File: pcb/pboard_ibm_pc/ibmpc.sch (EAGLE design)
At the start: 49 parts, among them IC1 STM32F072C8T6, SW1 324_SW, SW4 324_SW, U1 MAX3232

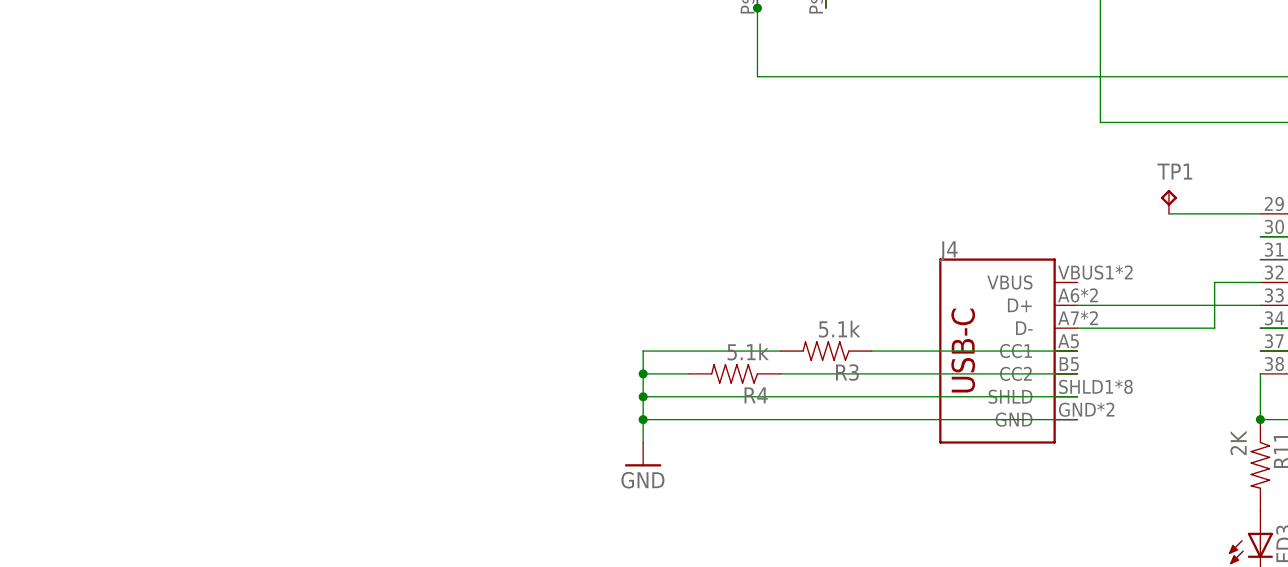
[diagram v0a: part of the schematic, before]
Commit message: finished ADB protocol board
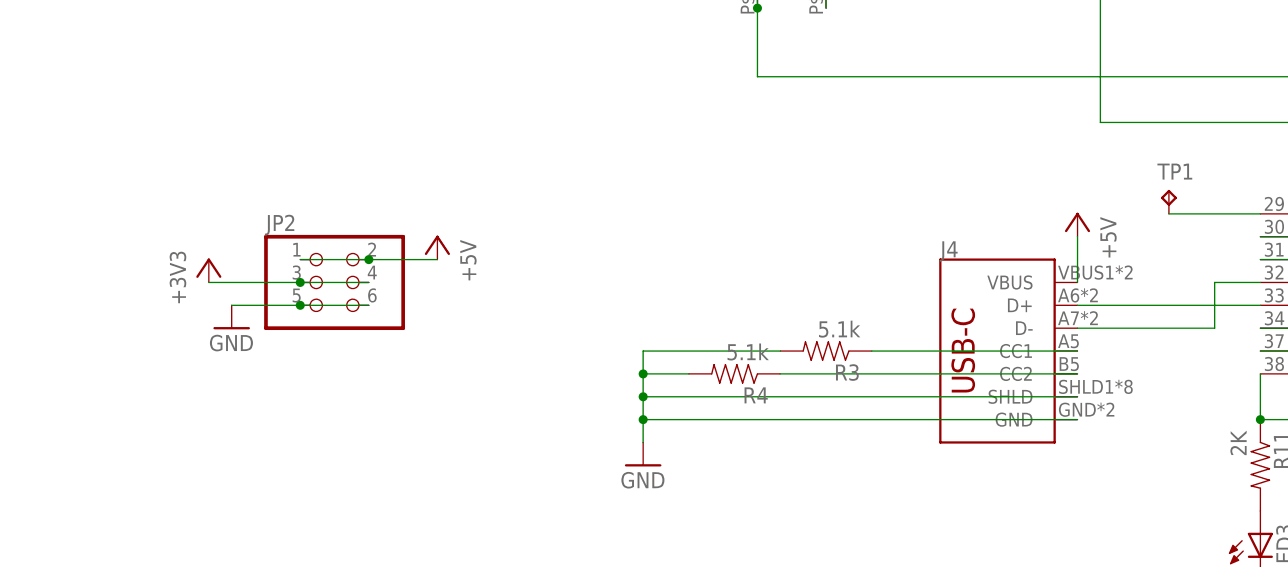
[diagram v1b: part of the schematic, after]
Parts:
- added JP2: (no value), pinhead:PINHD-2X3
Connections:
- net +3V3: now also JP2.3, JP2.4
- net +5V: now also J4.VBUS, JP2.1, JP2.2
- net GND: now also JP2.5, JP2.6
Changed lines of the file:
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@@
 <part name="+3V9" library="backplane" deviceset="+3V3" device=""/>
 <part name="+3V12" library="backplane" deviceset="+3V3" device=""/>
+<part name="P+2" library="supply1" library_urn="urn:adsk.eagle:library:371" deviceset="+5V" device=""/>
+<part name="JP2" library="pinhead" library_urn="urn:adsk.eagle:library:325" deviceset="PINHD-2X3" device="" package3d_urn="urn:adsk.eagle:package:22462/2"/>
+<part name="P+3" library="supply1" library_urn="urn:adsk.eagle:library:371" deviceset="+5V" device=""/>
+<part name="GND17" library="supply1" library_urn="urn:adsk.eagle:library:371" deviceset="GND" device=""/>
+<part name="+3V13" library="supply1" library_urn="urn:adsk.eagle:library:371" deviceset="+3V3" device=""/>
 </parts>
 <sheets>
@@
 <attribute name="VALUE" x="139.7" y="172.72" size="1.778" layer="96"/>
 </instance>
+<instance part="P+2" gate="1" x="20.32" y="-38.1" smashed="yes" rot="MR0">
+<attribute name="VALUE" x="22.86" y="-43.18" size="1.778" layer="96" rot="MR90"/>
+</instance>
+<instance part="JP2" gate="A" x="-63.5" y="-45.72" smashed="yes">
+<attribute name="NAME" x="-69.85" y="-40.005" size="1.778" layer="95"/>
+<attribute name="VALUE" x="-69.85" y="-53.34" size="1.778" layer="96"/>
+</instance>
+<instance part="P+3" gate="1" x="-50.8" y="-40.64" smashed="yes" rot="MR0">
+<attribute name="VALUE" x="-48.26" y="-45.72" size="1.778" layer="96" rot="MR90"/>
+</instance>
+<instance part="GND17" gate="1" x="-73.66" y="-50.8" smashed="yes">
+<attribute name="VALUE" x="-76.2" y="-53.34" size="1.778" layer="96"/>
+</instance>
+<instance part="+3V13" gate="G$1" x="-76.2" y="-43.18" smashed="yes">
+<attribute name="VALUE" x="-78.74" y="-48.26" size="1.778" layer="96" rot="R90"/>
+</instance>
 </instances>
 <busses>
@@
 <pinref part="+3V9" gate="G$1" pin="+3V3"/>
 <wire x1="106.68" y1="167.64" x2="111.76" y2="167.64" width="0.1524" layer="91"/>
+</segment>
+<segment>
+<pinref part="JP2" gate="A" pin="3"/>
+<pinref part="+3V13" gate="G$1" pin="+3V3"/>
+<wire x1="-66.04" y1="-45.72" x2="-76.2" y2="-45.72" width="0.1524" layer="91"/>
+<pinref part="JP2" gate="A" pin="4"/>
+<wire x1="-66.04" y1="-45.72" x2="-58.42" y2="-45.72" width="0.1524" layer="91"/>
+<junction x="-66.04" y="-45.72"/>
 </segment>
 </net>
@@
 <wire x1="20.32" y1="93.98" x2="20.32" y2="81.28" width="0.1524" layer="91"/>
 </segment>
+<segment>
+<pinref part="GND17" gate="1" pin="GND"/>
+<pinref part="JP2" gate="A" pin="5"/>
+<wire x1="-73.66" y1="-48.26" x2="-66.04" y2="-48.26" width="0.1524" layer="91"/>
+<pinref part="JP2" gate="A" pin="6"/>
+<wire x1="-66.04" y1="-48.26" x2="-58.42" y2="-48.26" width="0.1524" layer="91"/>
+<junction x="-66.04" y="-48.26"/>
+</segment>
 </net>
 <net name="N$29" class="0">
@@
 <junction x="114.3" y="43.18"/>
 </segment>
-</net>
+<segment>
+<pinref part="P+2" gate="1" pin="+5V"/>
+<pinref part="J4" gate="J1" pin="VBUS"/>
+<wire x1="20.32" y1="-40.64" x2="20.32" y2="-45.72" width="0.1524" layer="91"/>
+</segment>
+<segment>
+<pinref part="P+3" gate="1" pin="+5V"/>
+<pinref part="JP2" gate="A" pin="2"/>
+<wire x1="-50.8" y1="-43.18" x2="-58.42" y2="-43.18" width="0.1524" layer="91"/>
+<pinref part="JP2" gate="A" pin="1"/>
+<wire x1="-58.42" y1="-43.18" x2="-66.04" y2="-43.18" width="0.1524" layer="91"/>
+<junction x="-58.42" y="-43.18"/>
+</segment>
+</net>

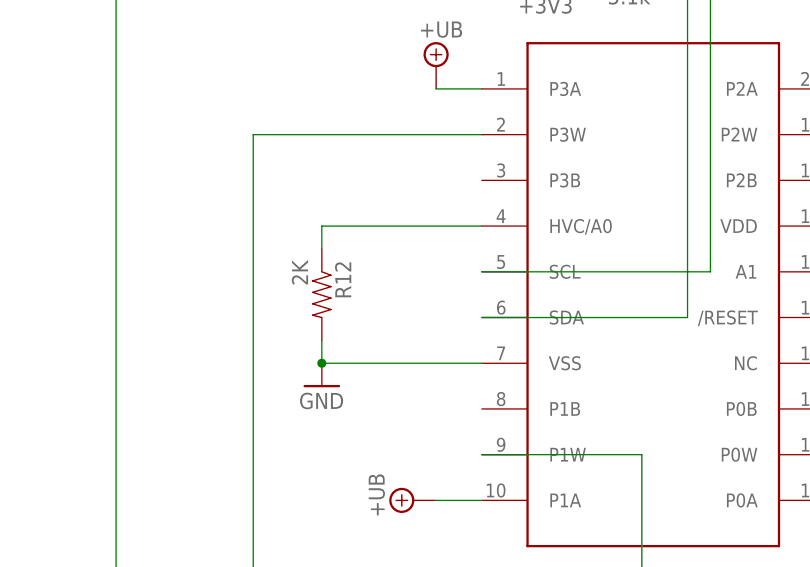
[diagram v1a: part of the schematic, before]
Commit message: added dsub stacker board
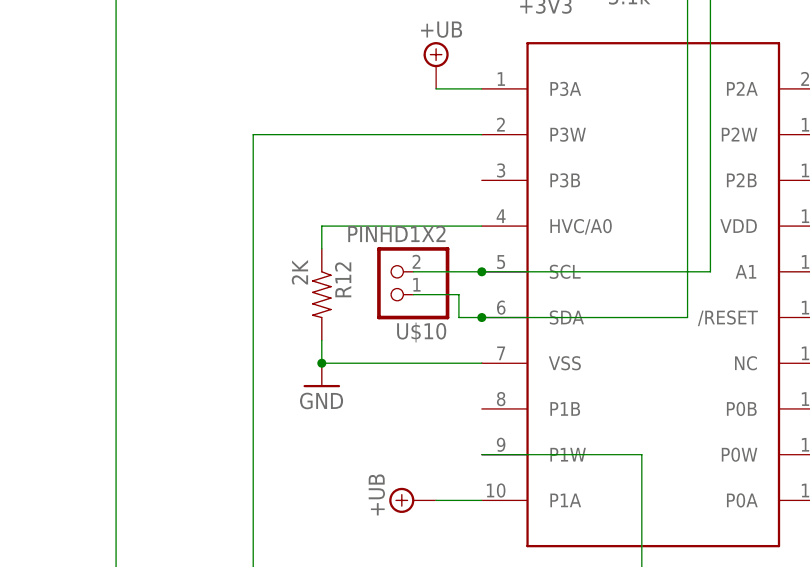
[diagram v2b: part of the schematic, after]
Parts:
- added U$10: PINHD1X2, adafruit_changed:PINHD1X2
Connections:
- removed net N$30: IC1PORTB_H.PB14, R14.2, U$6.SDA
- removed net N$31: IC1PORTB_H.PB13, R13.2, U$6.SCL
- new net POT_SCL: IC1PORTB_H.PB13, R13.2, U$10.2, U$6.SCL
- new net PST_SDA: IC1PORTB_H.PB14, R14.2, U$10.1, U$6.SDA
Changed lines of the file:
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@@
 <part name="GND17" library="supply1" library_urn="urn:adsk.eagle:library:371" deviceset="GND" device=""/>
 <part name="+3V13" library="supply1" library_urn="urn:adsk.eagle:library:371" deviceset="+3V3" device=""/>
+<part name="U$10" library="adafruit_changed" deviceset="PINHD1X2" device=""/>
 </parts>
 <sheets>
@@
 <attribute name="VALUE" x="-78.74" y="-48.26" size="1.778" layer="96" rot="R90"/>
 </instance>
+<instance part="U$10" gate="1" x="88.9" y="134.62" smashed="yes" rot="R180">
+<attribute name="NAME" x="95.25" y="128.905" size="1.778" layer="95" rot="R180"/>
+<attribute name="VALUE" x="95.25" y="139.7" size="1.778" layer="96" rot="R180"/>
+</instance>
 </instances>
 <busses>
@@
 </segment>
 </net>
-<net name="N$30" class="0">
+<net name="PST_SDA" class="0">
 <segment>
 <pinref part="IC1" gate="PORTB_H" pin="PB14"/>
@@
 <pinref part="R14" gate="G$1" pin="2"/>
 <junction x="121.92" y="167.64"/>
-</segment>
-</net>
-<net name="N$31" class="0">
+<wire x1="99.06" y1="129.54" x2="96.52" y2="129.54" width="0.1524" layer="91"/>
+<wire x1="96.52" y1="129.54" x2="96.52" y2="132.08" width="0.1524" layer="91"/>
+<junction x="99.06" y="129.54"/>
+<pinref part="U$10" gate="1" pin="1"/>
+<wire x1="96.52" y1="132.08" x2="91.44" y2="132.08" width="0.1524" layer="91"/>
+</segment>
+</net>
+<net name="POT_SCL" class="0">
 <segment>
 <pinref part="IC1" gate="PORTB_H" pin="PB13"/>
@@
 <pinref part="R13" gate="G$1" pin="2"/>
 <junction x="124.46" y="170.18"/>
-</segment>
-</net>
+<pinref part="U$10" gate="1" pin="2"/>
+<wire x1="99.06" y1="134.62" x2="91.44" y2="134.62" width="0.1524" layer="91"/>
+<junction x="99.06" y="134.62"/>
+</segment>
+</net>

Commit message: finishing touches for new boards
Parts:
- removed SW4: 324_SW, 3pos_slide_switch_centered:324_SW
- removed TP4: TPTP12R, testpad:TPTP12R
- added R15: 2K, SparkFun-Passives:RESISTOR0805-RES
- added SW2: 324_SW, 3pos_slide_switch_centered:324_SW
- C3: value 1uF -> 100nF
- C9: value 100nF -> 1uF
- J2: device SparkFun-Connectors:DIN7 -> SparkFun-Connectors:DB9MALE
- J3: device SparkFun-Connectors:DB9MALE -> SparkFun-Connectors:DIN7
- R1: value 12K -> 5.1k
- R11, R9: value 2K -> 12K
- R2: value 2K -> 5.1k
- R3, R4: value 5.1k -> 2K
- R5: value 12K -> 2K
- U$1: value GAMEPORT_15P -> PINHD1X4; device ibmpc:GAMEPORT_15P -> adafruit_changed:PINHD1X4
- U$10: value PINHD1X2 -> PINHD1X4; device adafruit_changed:PINHD1X2 -> adafruit_changed:PINHD1X4
- U$4: value M2.5HOLE -> PINHD1X2; device f1c100s:M2.5HOLE -> adafruit_changed:PINHD1X2
- U$5: value M2.5HOLE -> MCP4451; device f1c100s:M2.5HOLE -> ps2:MCP4451
- U$6: value MCP4451 -> M2.5HOLE; device ps2:MCP4451 -> f1c100s:M2.5HOLE
- U$7: value PINHD1X4 -> M2.5HOLE; device adafruit_changed:PINHD1X4 -> f1c100s:M2.5HOLE
- U$9: value PINHD1X4 -> GAMEPORT_15P; device adafruit_changed:PINHD1X4 -> ibmpc:GAMEPORT_15P
- renumbered JP4 to JP3
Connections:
- removed net N$35: U$1.Y1, U$6.P2W
- removed net N$36: U$1.Y2, U$6.P3W
- new net N$30: U$5.P1W, U$9.Y2
- new net N$31: IC1PORTF/OSC.PF1/OSC=>, R5.1, U$9.B1
- net +3V3: now also C1.1, C6.2, C7.2, C9.2, LED1.A, R1.1, R2.1, R3.1, R9.2, SW2.2, SW2.3, U$5.VDD; no longer C1.2, C2.2, C3.2, C7.1, LED2.A, R1.2, R13.1, R14.1, SW1.2, SW1.3, U$6.VDD
- net +UB: now also R5.2, R6.2, U$5.P0A, U$5.P1A, U$5.P2A, U$5.P3A, U$9.5V_1, U$9.5V_2, U$9.5V_3; no longer R7.2, R9.2, U$1.5V_1, U$1.5V_2, U$1.5V_3, U$6.P0A, U$6.P1A, U$6.P2A, U$6.P3A
- net C1+: now also C3.1; no longer C9.1
- net C1-: now also C3.2; no longer C9.2
- net C2+: now also C5.1; no longer C4.1
- net C2-: now also C5.2; no longer C4.2
- net GND: now also C1.2, C2.2, C4.2, C6.1, C7.1, C9.1, J2.5, J3.3_GND, LED2.C, R11.1, R13.2, R14.2, R7.1, SW1.1, SW1.4, U$1.4, U$5.A1, U$5.VSS, U$9.GND_B1, U$9.GND_B2; no longer C1.1, C2.1, C3.1, C5.2, C6.2, C7.2, J2.3_GND, J3.5, LED1.C, R12.2, R3.2, R5.1, R6.1, SW4.1, SW4.4, U$1.GND_B1, U$1.GND_B2, U$6.A1, U$6.VSS, U$7.4
- net N$1: now also R13.1; no longer R3.1
- net N$10: now also J1.1_DATA, U$1.2; no longer J2.1_DATA, U$8.2
- net N$11: now also J1.5_CLK, U$1.3; no longer J2.5_CLK, U$8.3
- net N$13: now also R9.1, SW1.2, SW1.3; no longer R1.1, SW4.2, SW4.3
- net N$17: now also U$5.P0W, U$9.Y1; no longer IC1PORTC.PC14, R7.1, U$1.B1
- net N$18: now also R11.2, SW2.1, SW2.4; no longer R5.2, SW1.1, SW1.4
- net N$19: now also IC1PORTC.PC15, R6.1, U$9.B2; no longer IC1PORTF/OSC.PF0/OSC<=, R8.1, U$1.B2
- net N$2: now also LED2.A, R12.2; no longer LED1.A, R2.2
- net N$20: now also IC1PORTF/OSC.PF0/OSC<=, R8.1, U$9.B3; no longer IC1PORTC.PC15, R9.1, U$1.B3
- net N$21: now also IC1PORTC.PC14, U$9.B4; no longer IC1PORTF/OSC.PF1/OSC=>, U$1.B4
- net N$25: now also J2.8; no longer J3.8
- net N$26: now also J3.1_DATA, U$8.2; no longer J1.1_DATA, U$7.2
- net N$27: now also R15.1; no longer R11.1
- net N$28: now also R15.2; no longer R11.2
- net N$29: now also LED1.C, R7.2; no longer LED2.C, R6.2
- net N$3: now also J3.4_5V, U$8.1; no longer J1.4_5V, U$7.1
- net N$32: now also R4.1, U$5.HVC/A0; no longer R12.1, U$6.HVC/A0
- net N$33: now also U$5.P2W, U$9.X2; no longer U$1.X1, U$6.P0W
- net N$34: now also U$5.P3W, U$9.X1; no longer U$1.X2, U$6.P1W
- net N$38: now also U$10.1; no longer U$9.1
- net N$39: now also U$10.2; no longer U$9.2
- net N$4: now also J1.4_5V, U$1.1; no longer J2.4_5V, U$8.1
- net N$40: now also U$10.3; no longer U$9.3
- net N$41: now also U$10.4; no longer U$9.4
- net N$44: now also R3.2, U$5./RESET; no longer TP4.TP
- net N$5: now also J3.5_CLK, U$8.3; no longer J1.5_CLK, U$7.3
- net N$6: now also R12.1; no longer R2.1
- net N$7: now also R14.1; no longer R4.1
- net POT_SCL: now also R1.2, U$4.2, U$5.SCL; no longer R13.2, U$10.2, U$6.SCL
- net PST_SDA: now also R2.2, U$4.1, U$5.SDA; no longer R14.2, U$10.1, U$6.SDA
- net RTS_HV: now also J2.7; no longer J3.7
- net STM32_RX_HV: now also J2.3; no longer J3.3
- net STM32_TX_HV: now also J2.2; no longer J3.2
- net V+: now also C2.1; no longer C6.1
- net V-: now also C4.1; no longer C5.1
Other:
- moved on the sheet: C1, C2, C3, C4, C5, C6, C7, C8, C9, J1, LED1, LED2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

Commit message: gamepad implemented on ibm board, analoge axes doesnt seem to be working correctly
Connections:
- net N$17 renamed Y1_W0
- net N$30 renamed Y2_W1
- net N$33 renamed X2_W2
- net N$34 renamed X1_W3
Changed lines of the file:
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@@
 </segment>
 </net>
-<net name="N$17" class="0">
+<net name="Y1_W0" class="0">
 <segment>
 <pinref part="U$9" gate="G$1" pin="Y1"/>
@@
 </segment>
 </net>
-<net name="N$30" class="0">
+<net name="Y2_W1" class="0">
 <segment>
 <pinref part="U$5" gate="G$1" pin="P1W"/>
@@
 </segment>
 </net>
-<net name="N$33" class="0">
+<net name="X2_W2" class="0">
 <segment>
 <pinref part="U$5" gate="G$1" pin="P2W"/>
@@
 </segment>
 </net>
-<net name="N$34" class="0">
+<net name="X1_W3" class="0">
 <segment>
 <pinref part="U$5" gate="G$1" pin="P3W"/>
